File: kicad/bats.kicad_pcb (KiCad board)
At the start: 2 copper layers, 68.9 x 53.6 mm, 30 parts, among them P1 SERVO, SW1 RESET, SW2 SHOT, SW4 LEFT, SW6 RIGHT, U1 BUZZER

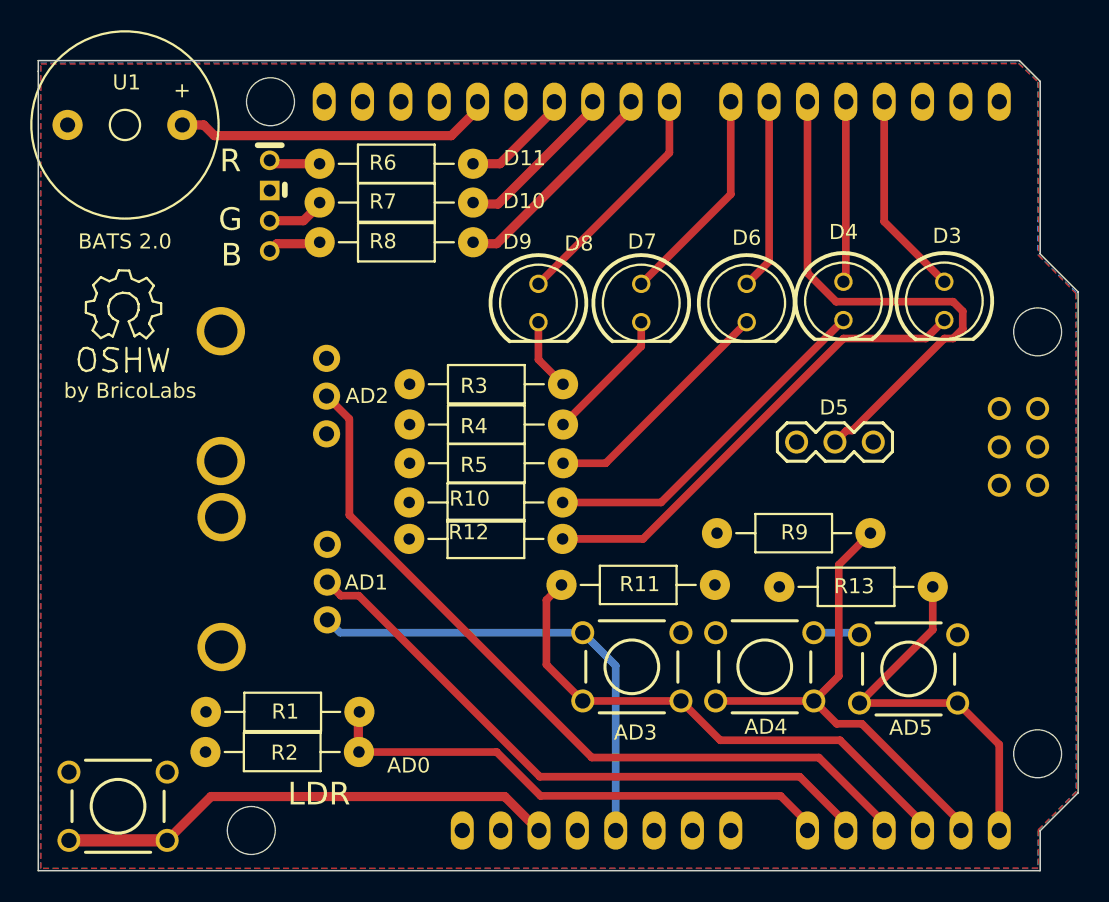
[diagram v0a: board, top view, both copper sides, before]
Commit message: Engadida a biblioteca KiCAD de BricoLabs coma submodule
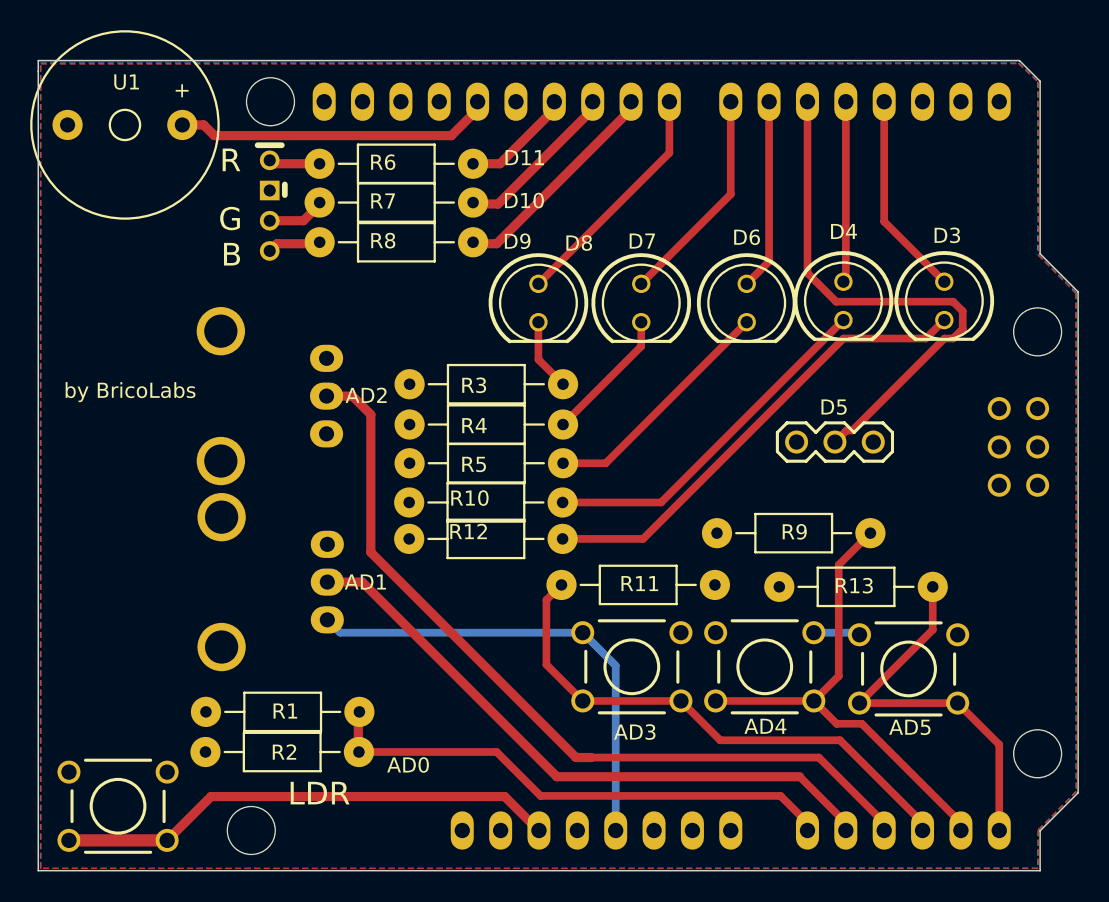
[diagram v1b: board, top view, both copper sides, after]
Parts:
- removed BATS 2.0: Symbol_OSHW-Logo_SilkScreen, Symbols:Symbol_OSHW-Logo_SilkScreen
- removed G***: LOGO, silklibrary:bat_b
- VR1, VR2: footprint FT:POT_RV09_VERT -> bl_kicad:POT_RV09_VERT_easySoldering
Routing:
- net /AD2: track 52.9 -> 54.5 mm

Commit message: Engadidas as novas pisadas "easy soldering" dende a biblioteca KiCAD de BricoLabs Actualizados os submódulos
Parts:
- LED1, LED2, LED3, LED5, LED6: footprint FT:LED-5MM -> bl_kicad:LED-5MM_easy_soldering
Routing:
- net /ARD5: track 35.4 -> 23.3 mm

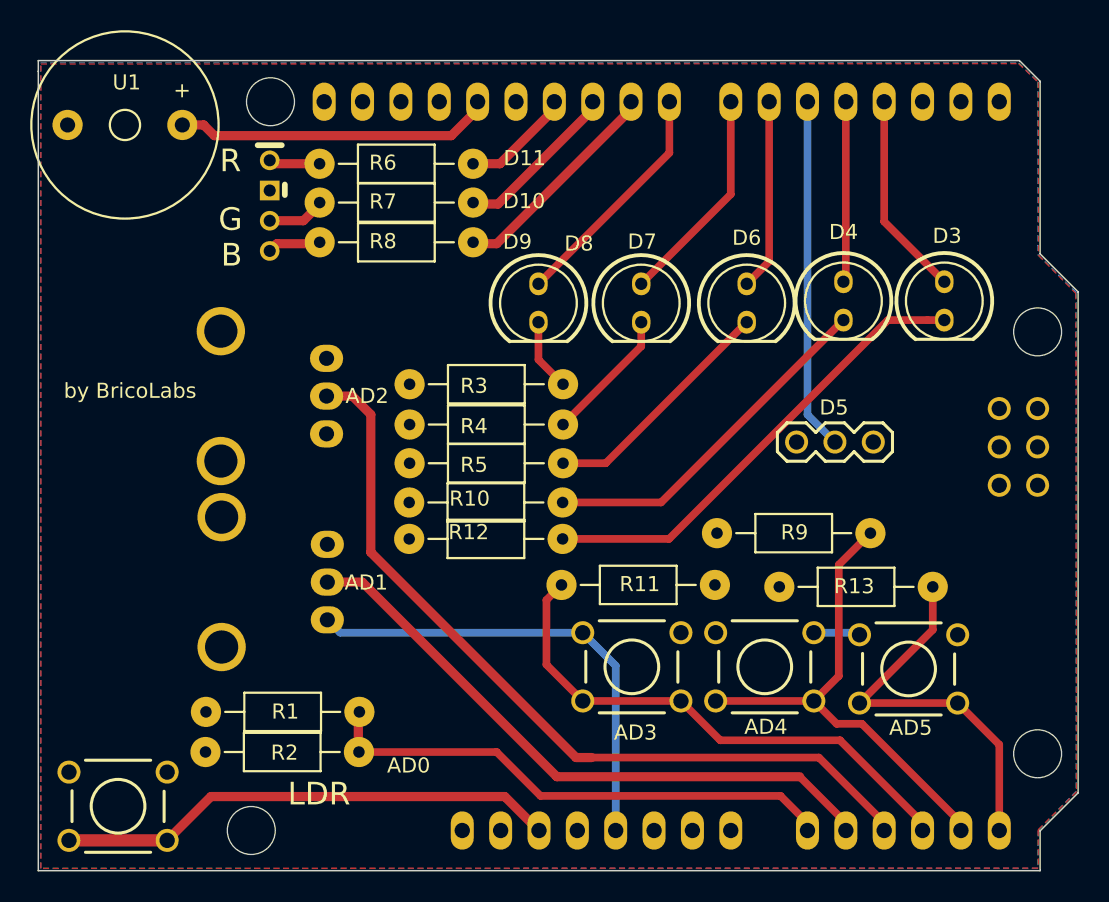
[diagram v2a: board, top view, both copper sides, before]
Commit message: Cambiadas as posicións dos botóns
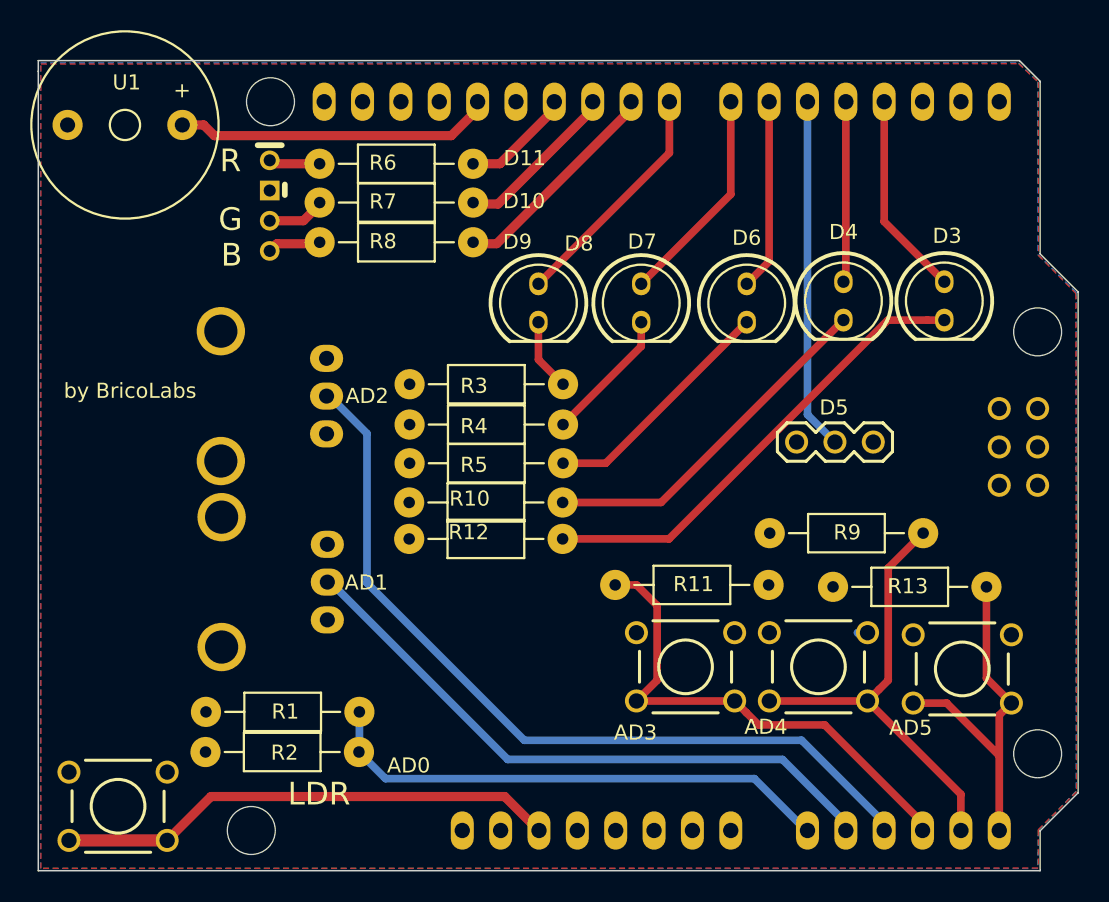
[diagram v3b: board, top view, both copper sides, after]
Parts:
- moved R11 3.56 mm to (165.0, 119.0)
- moved SW2 3.56 mm to (178.5, 124.4)
- moved R13 3.56 mm to (189.6, 119.1)
- moved SW4 3.56 mm to (169.7, 124.4)
- moved SW6 3.56 mm to (188.0, 124.6)
- moved R9 3.49 mm to (185.4, 115.6)
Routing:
- net /VCC: track 34.3 -> 0.20 mm
- net /AD3: track 35.4 -> 33.0 mm
- net /AD4: track 32.8 -> 30.8 mm
- net /AD5: track 25.8 -> 24.3 mm
- net /AD2: track 54.5 -> 55.5 mm
- net /AD1: track 41.4 -> 42.0 mm
